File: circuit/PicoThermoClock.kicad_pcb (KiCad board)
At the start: 4 copper layers, 100 x 100 mm, 42 parts, among them J1 USB_B_Micro, J2 AVR-ISP-6, J3 Conn_01x03, J4 Conn_01x03, Q1 SS9012H, Q2 SS9012H, Q3 SS9012H, Q4 SS9012H, Q5 C1815GR, SW1 SW_Push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

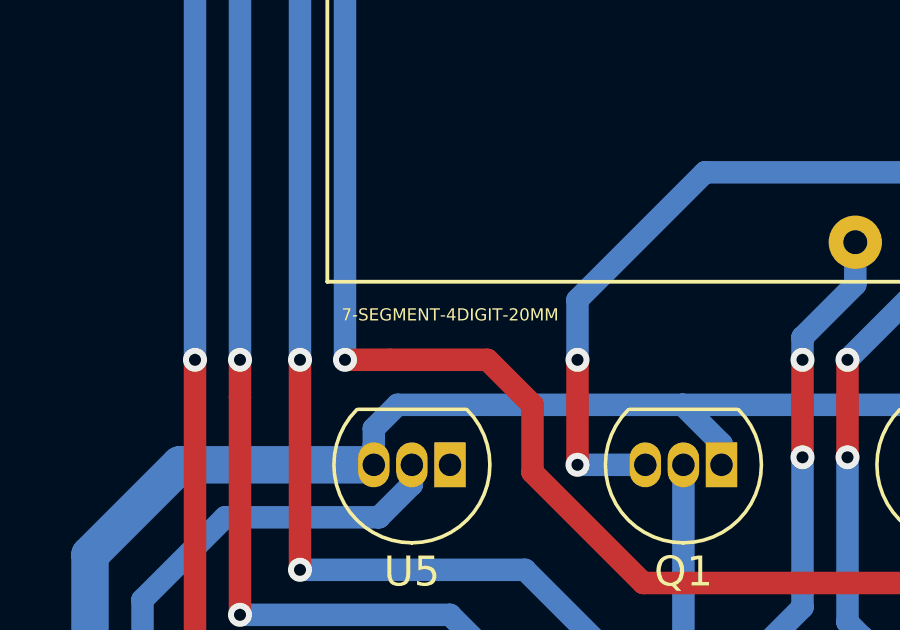
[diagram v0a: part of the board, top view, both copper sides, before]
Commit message: Apply changed footprint to the pcb
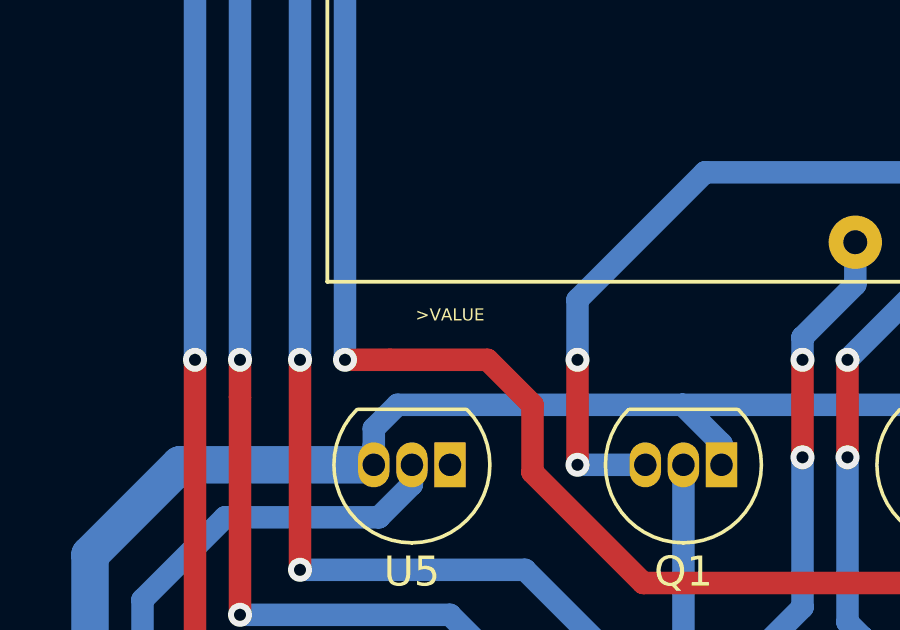
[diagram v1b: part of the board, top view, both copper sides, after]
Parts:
- LED1: value 7-SEGMENT-4DIGIT-20MM -> >VALUE
